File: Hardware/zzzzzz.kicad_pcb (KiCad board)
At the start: 2 copper layers, 0 parts

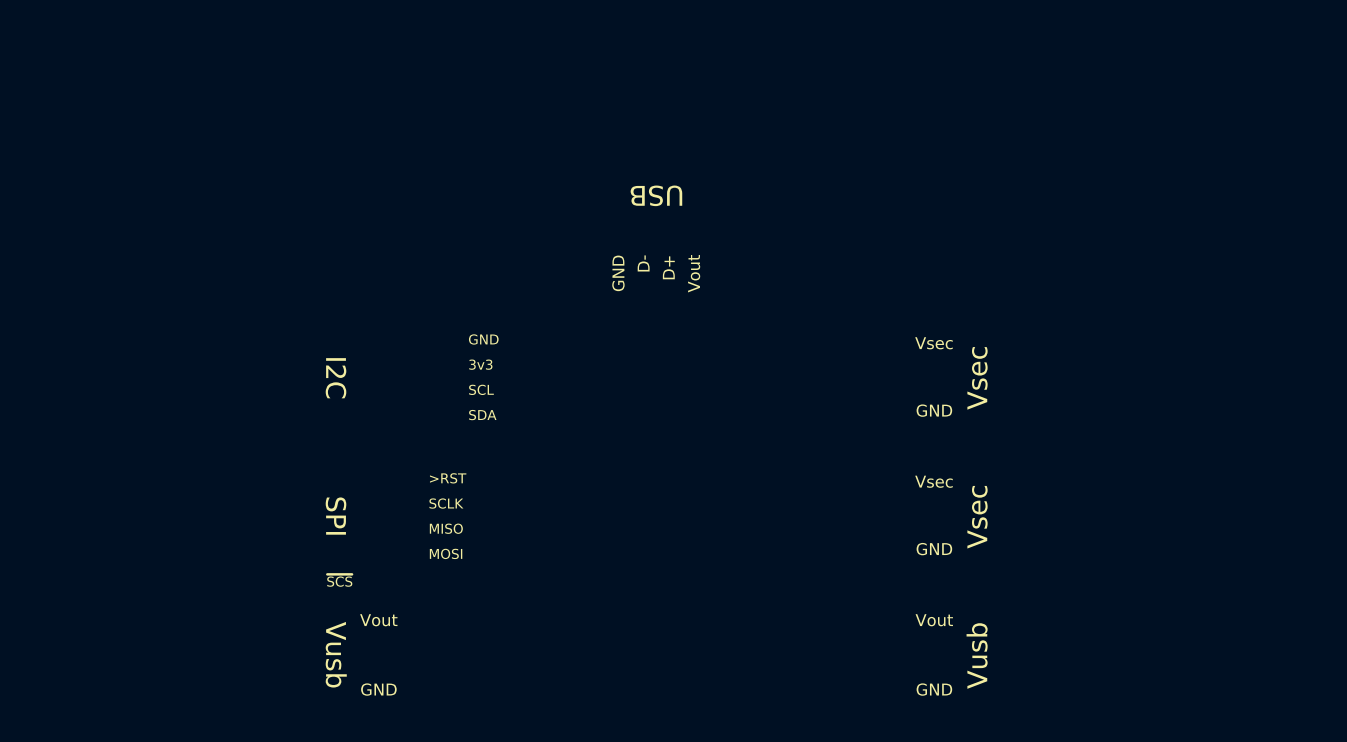
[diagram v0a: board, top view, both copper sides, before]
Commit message: Still working on changes to J7/J9...
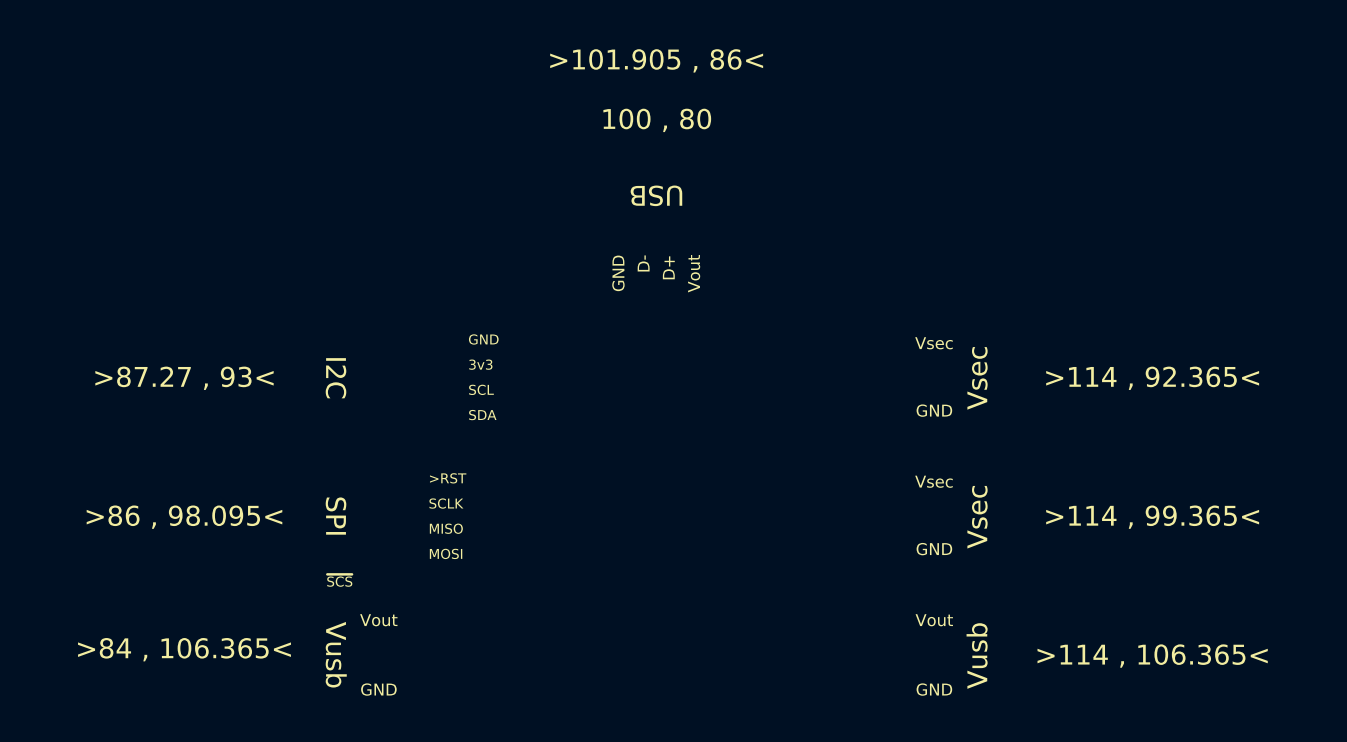
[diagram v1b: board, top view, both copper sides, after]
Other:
- board text added: "100 , 80"
- board text added: ">101.905 , 86<"
- board text added: ">114 , 106.365<"
- board text added: ">114 , 92.365<"
- board text added: ">114 , 99.365<"
- board text added: ">84 , 106.365<"
- board text added: ">86 , 98.095<"
- board text added: ">87.27 , 93<"
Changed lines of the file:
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@@
     (effects (font (size 0.5 0.5) (thickness 0.125)) (justify left))
+  )
+  (gr_text "100 , 80" (at 100 80) (layer "F.SilkS")
+    (effects (font (size 1 1) (thickness 0.15)))
   )
   (gr_text "Vout" (at 114 105.245) (layer "F.SilkS")
@@
     (effects (font (size 0.5 0.5) (thickness 0.125)) (justify left))
   )
+  (gr_text ">86 , 98.095<" (at 76.2 100) (layer "F.SilkS")
+    (effects (font (size 1 1) (thickness 0.15)))
+  )
   (gr_text "GND" (at 114 94.685) (layer "F.SilkS")
     (effects (font (size 0.6 0.6) (thickness 0.125)))
@@
   (gr_text "GND" (at 90.5 91.095) (layer "F.SilkS")
     (effects (font (size 0.5 0.5) (thickness 0.125)) (justify left))
+  )
+  (gr_text ">101.905 , 86<" (at 100 77) (layer "F.SilkS")
+    (effects (font (size 1 1) (thickness 0.15)))
+  )
+  (gr_text ">114 , 106.365<" (at 125 107) (layer "F.SilkS")
+    (effects (font (size 1 1) (thickness 0.15)))
   )
   (gr_text "D-" (at 99.365 86.8 90) (layer "F.SilkS")
@@
     (effects (font (size 0.5 0.5) (thickness 0.125)) (justify left))
   )
+  (gr_text ">114 , 92.365<" (at 125 93) (layer "F.SilkS")
+    (effects (font (size 1 1) (thickness 0.15)))
+  )
   (gr_text "GND" (at 114 108.745) (layer "F.SilkS")
     (effects (font (size 0.6 0.6) (thickness 0.125)))
+  )
+  (gr_text ">84 , 106.365<" (at 76.2 106.68) (layer "F.SilkS")
+    (effects (font (size 1 1) (thickness 0.15)))
   )
   (gr_text "I2C" (at 83.8 93 -90) (layer "F.SilkS")
@@
     (effects (font (size 0.6 0.6) (thickness 0.125)))
   )
+  (gr_text ">87.27 , 93<" (at 76.2 93) (layer "F.SilkS")
+    (effects (font (size 1 1) (thickness 0.15)))
+  )
   (gr_text "Vout" (at 86 105.245) (layer "F.SilkS")
     (effects (font (size 0.6 0.6) (thickness 0.125)))
@@
     (effects (font (size 0.6 0.6) (thickness 0.125)))
   )
+  (gr_text ">114 , 99.365<" (at 125 100) (layer "F.SilkS")
+    (effects (font (size 1 1) (thickness 0.15)))
+  )
 )
